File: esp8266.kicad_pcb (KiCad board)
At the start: 2 copper layers, 55.1 x 26 mm, 39 parts, among them J1 Conn_01x08, J2 Conn_01x08, Q1 AO3401A, U10 TS-1187A-B-A-B, U11 W25Q128JVSIQTR, U13 CH340C, U2 ESP8266EX, U3 AP2112K-3_3TRG1, U4 HDC1080DMBR, U5 MCP73831T-2ACI_OT, U6 MK-12C02-G020, U7 S2B-PH-SM4-TB(LF)(SN), U8 SK6812MINI-HS, U9 UMH3N, Y1 26Mhz

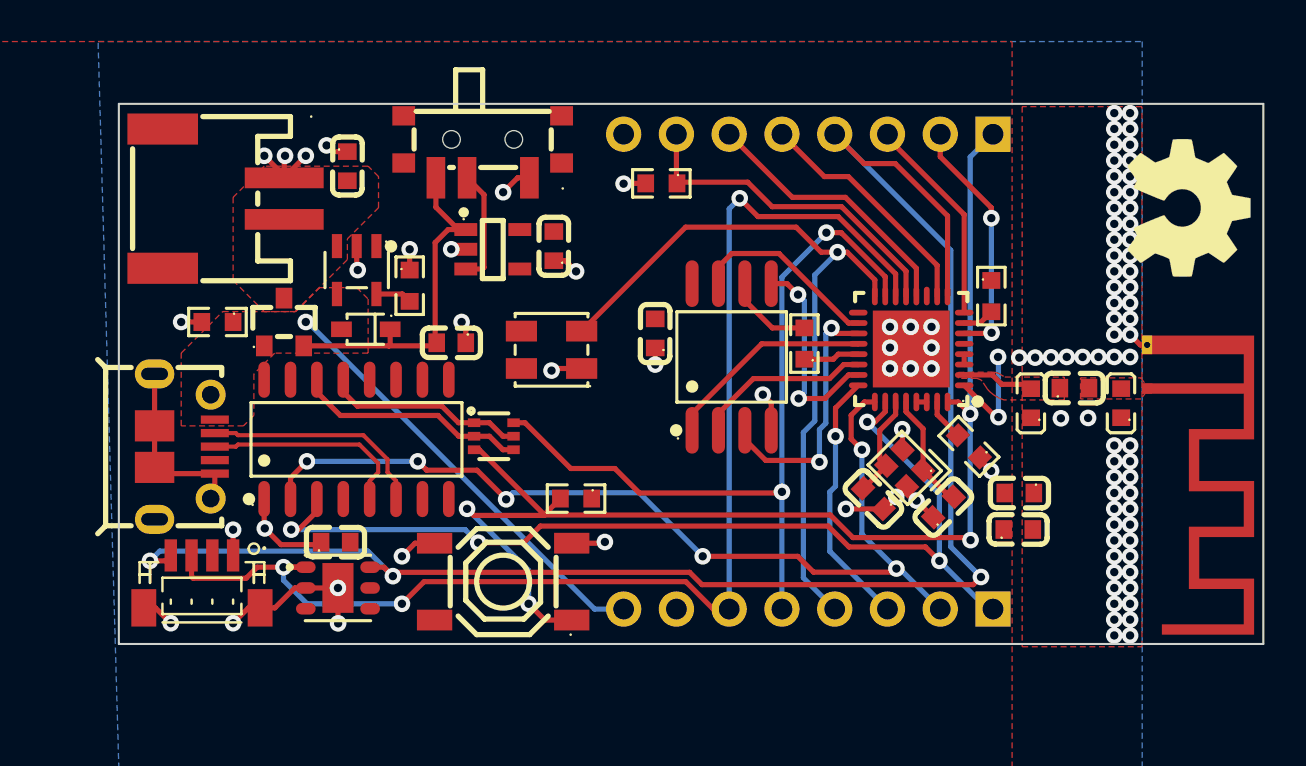
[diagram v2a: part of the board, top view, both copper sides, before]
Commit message: Add silkscreen, test points and optional pull ups for I2C
Also don’t route underneath antenna pin
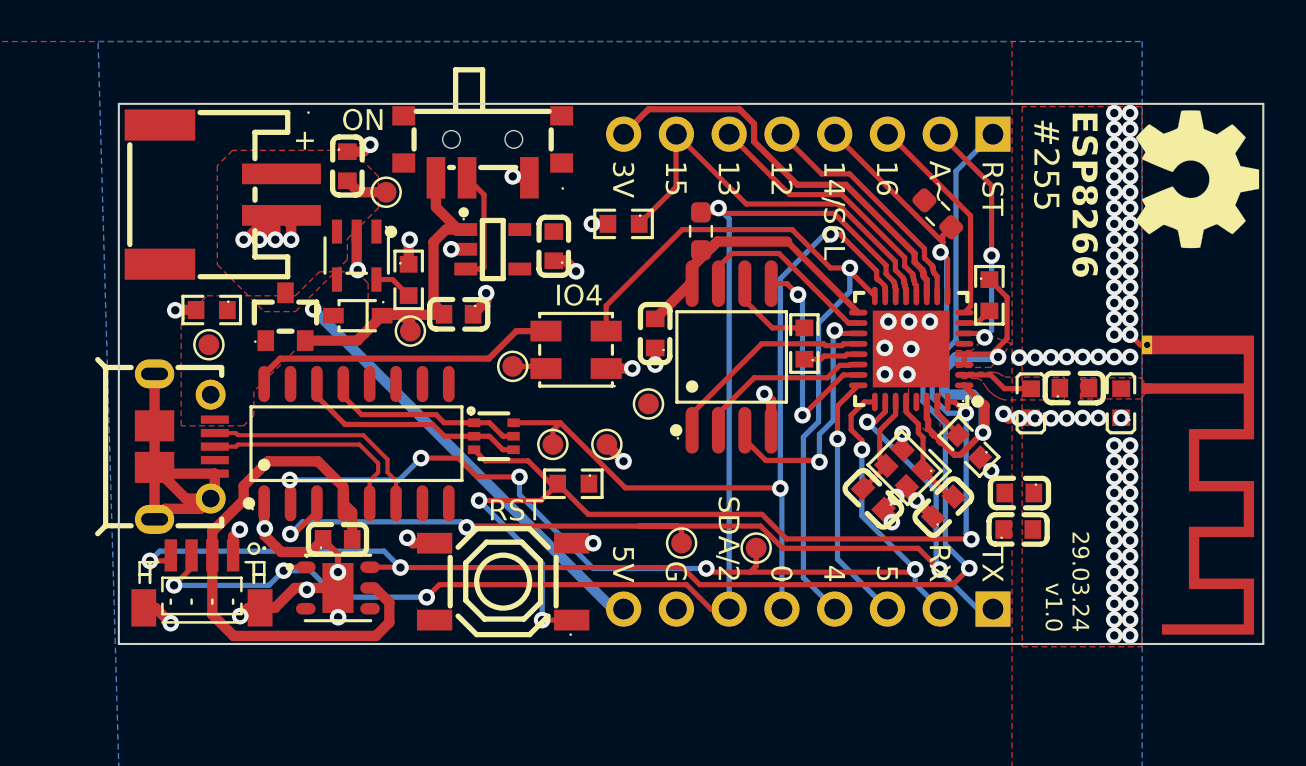
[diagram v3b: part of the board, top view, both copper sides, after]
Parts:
- added R8: 2k, Resistor_SMD:R_0603_1608Metric_Pad0.98x0.95mm_HandSolder, F.Cu at (86.0, 129.1)
- added R9: 2k, Resistor_SMD:R_0603_1608Metric_Pad0.98x0.95mm_HandSolder, F.Cu at (97.4, 128.3)
- added TP1: TestPoint, TestPoint:TestPoint_Pad_D1.0mm, F.Cu at (77.0, 135.6)
- added TP2: TestPoint, TestPoint:TestPoint_Pad_D1.0mm, F.Cu at (85.1, 144.1)
- added TP3: TestPoint, TestPoint:TestPoint_Pad_D1.0mm, F.Cu at (88.7, 144.4)
- added TP4: TestPoint, TestPoint:TestPoint_Pad_D1.0mm, F.Cu at (78.9, 139.4)
- added TP5: TestPoint, TestPoint:TestPoint_Pad_D1.0mm, F.Cu at (81.5, 139.4)
- added TP6: TestPoint, TestPoint:TestPoint_Pad_D1.0mm, F.Cu at (72.0, 133.9)
- added TP7: TestPoint, TestPoint:TestPoint_Pad_D1.0mm, F.Cu at (62.3, 134.6)
- added TP8: TestPoint, TestPoint:TestPoint_Pad_D1.0mm, F.Cu at (83.5, 137.4)
- added TP9: TestPoint, TestPoint:TestPoint_Pad_D1.0mm, F.Cu at (70.9, 127.3)
- OSHW1: value github.com/besi/stepomatic -> locked
- U10: value TS-1187A-B-A-B -> RST
- U6: value MK-12C02-G020 -> ON
- U7: value S2B-PH-SM4-TB(LF)(SN) -> +
- moved R6 2.67 mm to (82.3, 128.8)
- moved OSHW1 1.44 mm to (109.9, 126.6)
- moved C7 1.42 mm to (74.4, 133.1)
- moved U8 1.18 mm to (80.0, 134.8)
- moved D3 0.76 mm to (69.5, 133.2)
- moved R5 0.72 mm to (79.9, 141.3)
- moved U5 0.70 mm to (69.4, 130.3)
- moved R7 0.64 mm to (62.5, 132.9)
- moved R4 0.28 mm to (72.0, 131.5)
- moved Q1 0.27 mm to (66.0, 133.2)
- moved U7 0.23 mm to (62.9, 127.4)
- moved U13 0.21 mm to (69.4, 139.4)
- moved C8 0.17 mm to (68.5, 144.0)
- moved R3 0.10 mm to (99.9, 132.2)
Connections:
- net Net-(D3-K) renamed VIN
- U7 pad 1: GND -> +BATT
- U7 pad 2: +BATT -> GND
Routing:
- net +3V3: track 6.18 -> 96.9 mm
- net GND: track 55.7 -> 69.4 mm, vias 102 -> 110
- net GPIO14: track 78.7 -> 71.0 mm, vias 3 -> 4
- net GPIO15: track 16.4 -> 20.0 mm
- net U0TXD: track 47.9 -> 50.9 mm
- net U0RXD: track 45.7 -> 48.3 mm
- net +BATT: track 0.00 -> 2.10 mm
- net NEOPIXEL_OUT: track 0.00 -> 1.64 mm
- net GPIO4: track 36.5 -> 35.1 mm
- net RESET: track 60.2 -> 61.4 mm
- net GPIO2: track 61.5 -> 62.5 mm, vias 3 -> 4
- net GPIO0: track 38.0 -> 38.9 mm
- net SD_SI: track 10.1 -> 10.9 mm
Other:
- board text added: "#255"
- board text added: "0"
- board text added: "12"
- board text added: "13"
- board text added: "14/SCL"
- board text added: "15"
- board text added: "16"
- board text added: "2 / SDA"
- board text added: "29.03.24 v1.0"
- board text added: "3V"
- board text added: "4"
- board text added: "5"
- board text added: "5V"
- board text added: "A~"
- board text added: "ESP8266"
- board text added: "G"
- board text added: "IO4"
- board text added: "JLC:"
- board text added: "JLCJLCJLCJLC"
- board text added: "RST"
- board text added: "RX"
- board text added: "SCL / 14"
- board text added: "SDA/2"
- board text added: "TX"

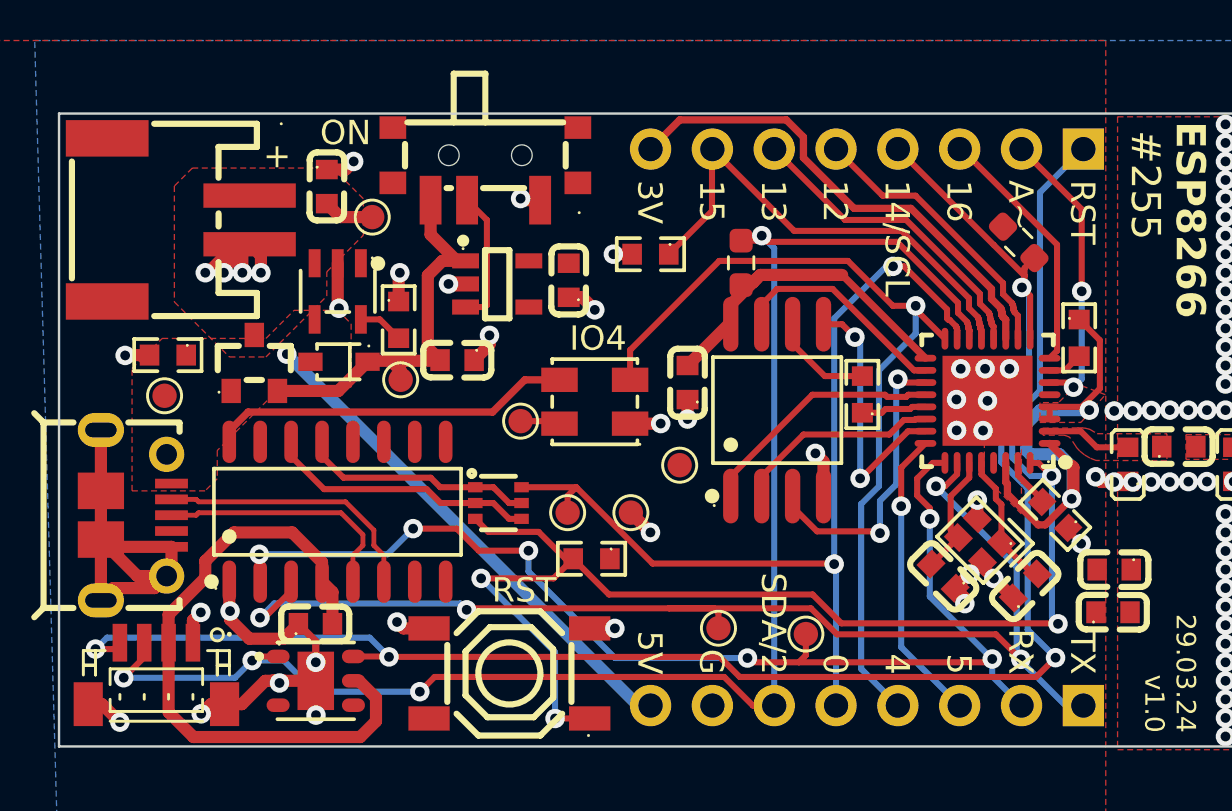
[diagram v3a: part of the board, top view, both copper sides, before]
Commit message: Add a solder jumper for IO16 and RESET
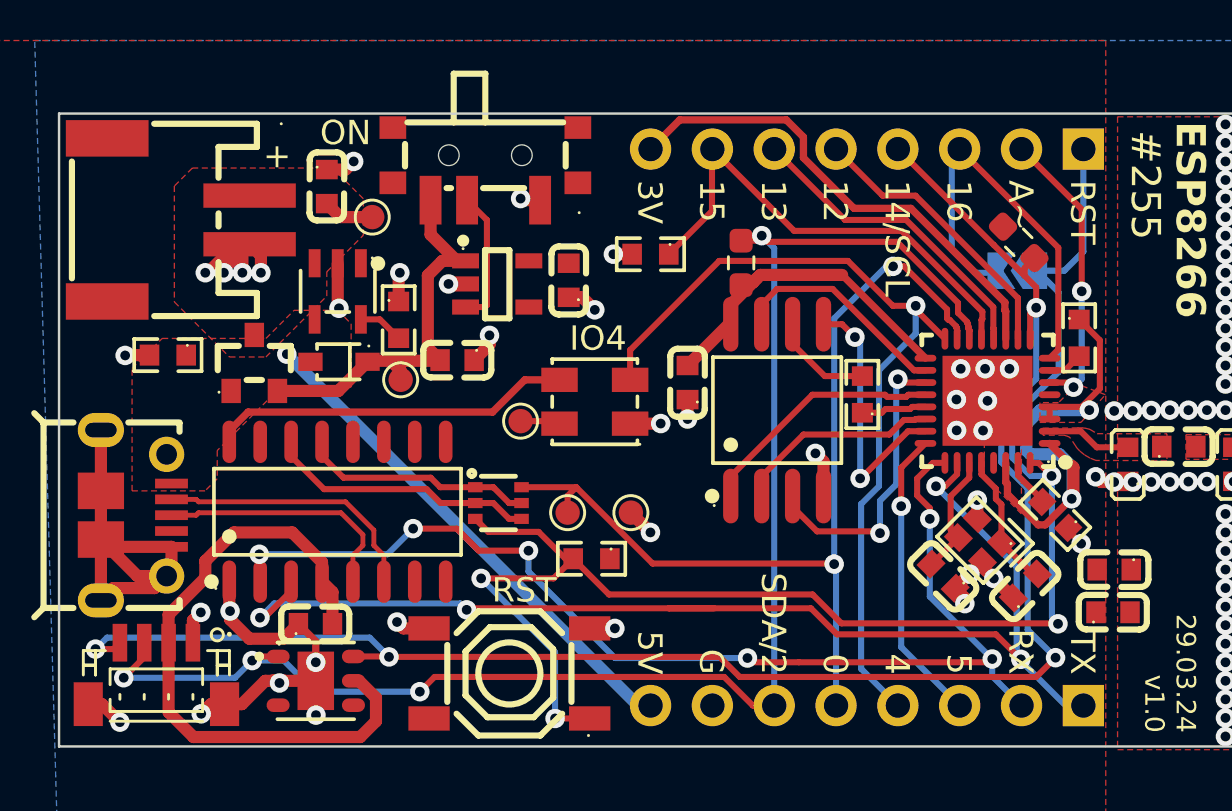
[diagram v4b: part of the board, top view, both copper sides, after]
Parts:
- removed TP2, TP3, TP7, TP8: TestPoint, TestPoint:TestPoint_Pad_D1.0mm
- added JP2: deep-sleep, Jumper:SolderJumper-2_P1.3mm_Open_TrianglePad1.0x1.5mm, B.Cu at (97.4, 129.5)
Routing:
- net GPIO16: track 10.4 -> 17.1 mm
- net RESET: track 61.4 -> 62.9 mm
- net U0RXD: track 48.3 -> 47.0 mm
- net U0TXD: track 50.9 -> 50.0 mm
- net GPIO14: track 71.0 -> 70.2 mm

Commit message: Prepare for production
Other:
- board text added: "29.03.24 e483d9 v1.0"
- board text removed: "29.03.24 v1.0"
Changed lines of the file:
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@@
     (effects (font (size 1.2 1.2) (thickness 0.1)) (justify left bottom))
   )
-  (gr_text "29.03.24\nv1.0\n" (at 102.52466 148.439238 270) (layer "F.SilkS")
+  (gr_text "29.03.24\ne483d9\nv1.0" (at 101.748067 148.735457 270) (layer "F.SilkS")
     (effects (font (size 0.8 0.8) (thickness 0.15)) (justify right bottom))
   )

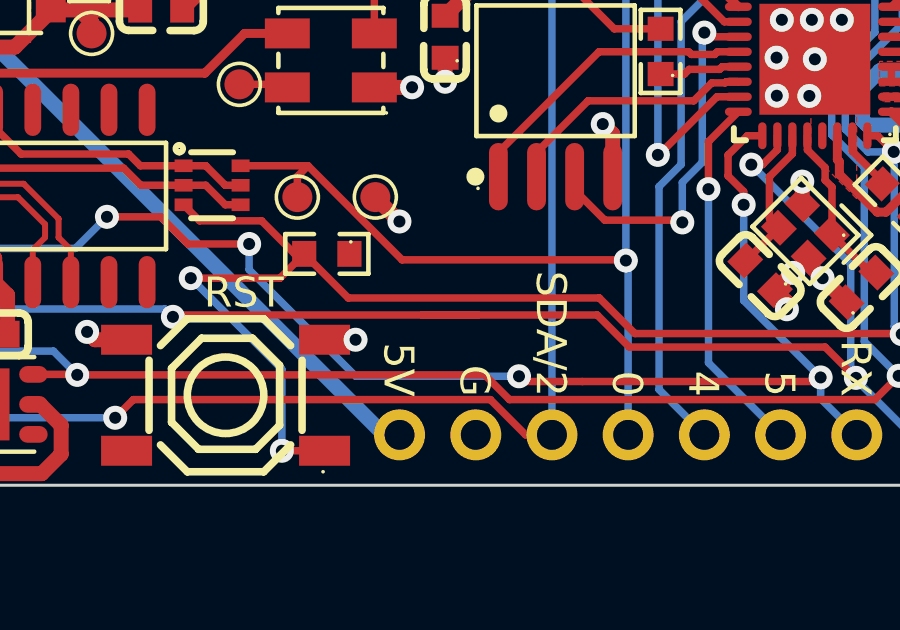
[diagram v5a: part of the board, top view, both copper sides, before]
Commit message: Don’t add solder jumper to BOM
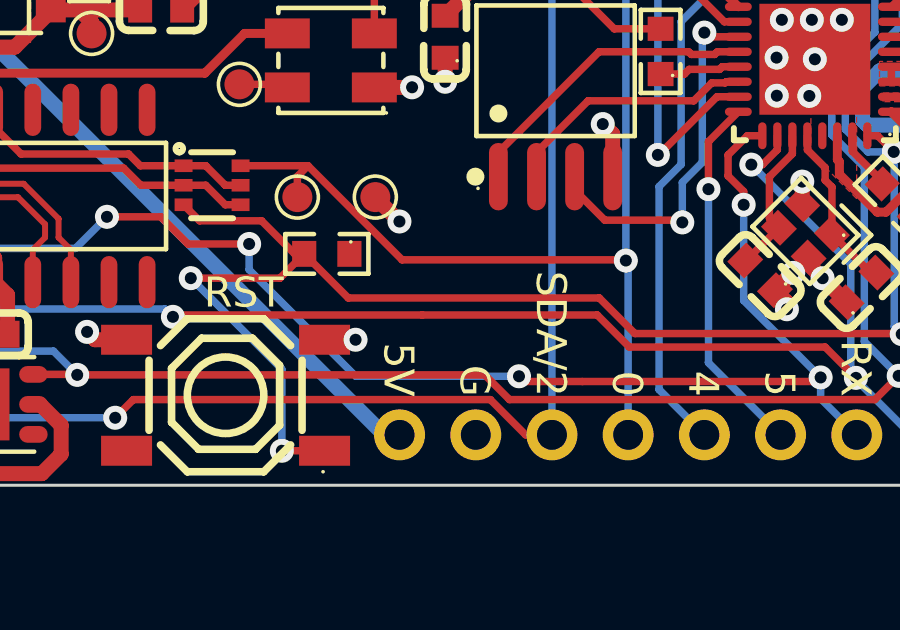
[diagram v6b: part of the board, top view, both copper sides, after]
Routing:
- net U0TXD: track 50.0 -> 48.1 mm
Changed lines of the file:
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@@
     (property "Sheetfile" "esp8266.kicad_sch")
     (property "Sheetname" "")
+    (property "exclude_from_bom" "")
     (property "ki_description" "Solder Jumper, 2-pole, open")
     (property "ki_keywords" "solder jumper SPST")
-    (attr exclude_from_pos_files)
+    (attr exclude_from_pos_files exclude_from_bom)
     (fp_text reference "JP2" (at 0 1.8) (layer "B.SilkS") hide
         (effects (font (size 1 1) (thickness 0.15)) (justify mirror))
@@
   (segment (start 94.893419 137.350309) (end 94.893419 137.817538) (width 0.25) (layer "F.Cu") (net 56))
   (segment (start 97.511853 145.42) (end 96.485739 144.393886) (width 0.25) (layer "F.Cu") (net 56))
-  (segment (start 84.904784 143.324784) (end 83.058 143.324784) (width 0.25) (layer "F.Cu") (net 56))
   (segment (start 89.958314 144.393886) (end 88.889212 143.324784) (width 0.25) (layer "F.Cu") (net 56))
   (segment (start 94.398424 138.312533) (end 94.02583 138.312533) (width 0.25) (layer "F.Cu") (net 56))
